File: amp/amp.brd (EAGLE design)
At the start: 99.1 x 80 mm, 81 parts, among them IC1 OPA2134PA, Q1 BC547, Q10 BC547, Q11 IRF540, Q12 IRF540, Q13 BC547, Q14 BC556, Q15 BC547, Q16 BC556, Q17 2N7000, Q18 BC547, Q19 BC547, Q2 BC556, Q20 BC547, Q21 BC547, Q22 BC547, Q23 IRF540, Q24 IRF540, Q3 BC547, Q4 BC556, Q5 2N7000, Q6 BC547, Q7 BC547, Q8 BC547, Q9 BC547

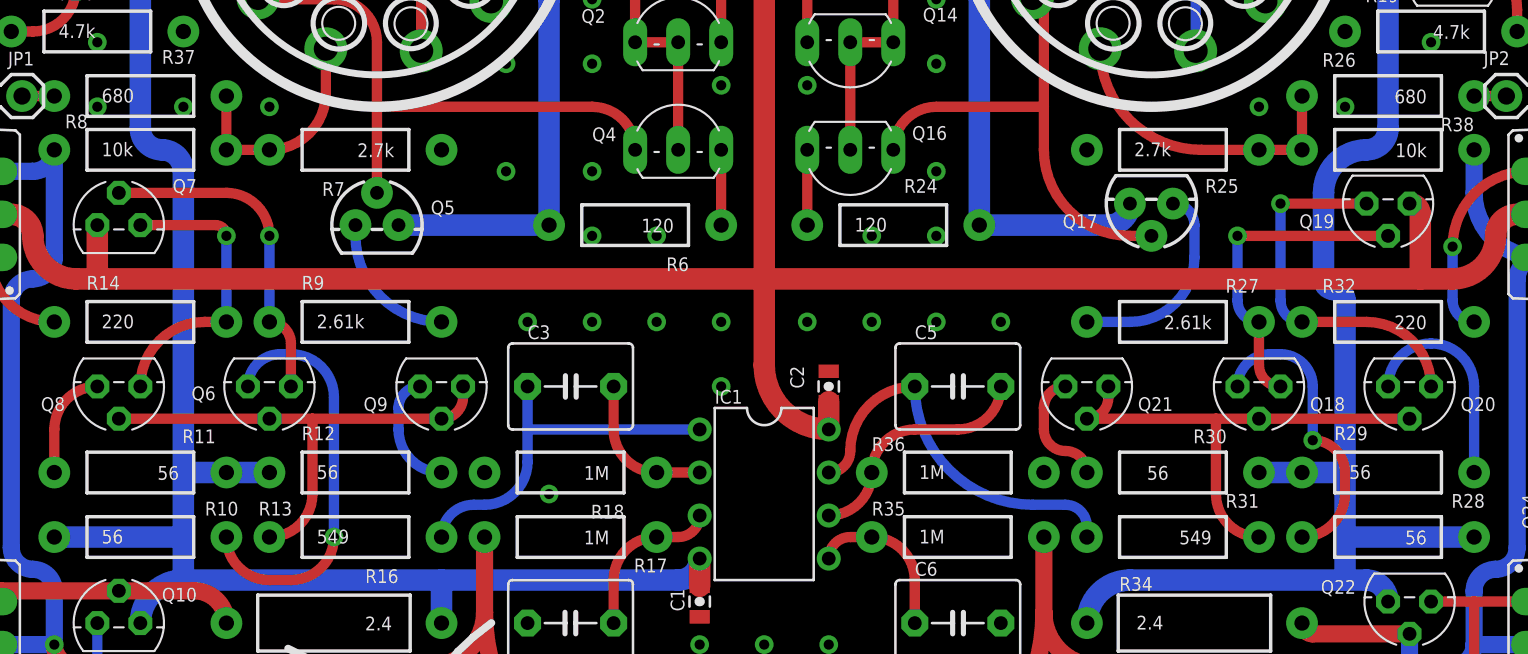
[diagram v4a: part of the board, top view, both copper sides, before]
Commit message: Some components changed
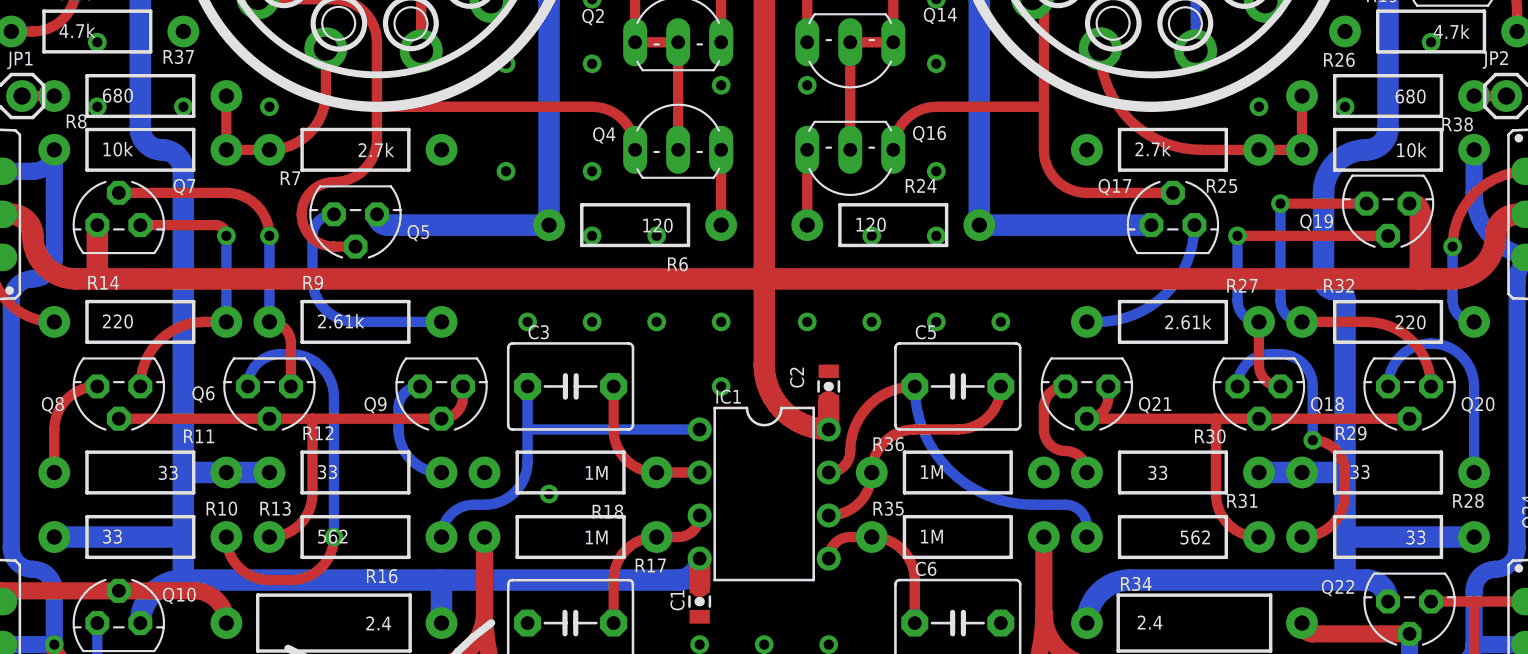
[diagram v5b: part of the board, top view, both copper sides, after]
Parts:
- Q1, Q10, Q13, Q15, Q18, Q19, Q20, Q21, Q22, Q3, Q6, Q7, Q8, Q9: value BC547 -> BC550C
- Q11, Q12, Q23, Q24: value IRF540 -> IRF510
- Q14, Q16, Q2, Q4: value BC556 -> BC560C
- Q17, Q5: value 2N7000 -> BC550C; device SparkFun-DiscreteSemi:TO-92 -> transistor-npn:TO92
- R10, R11, R12, R28, R29, R30: value 56 -> 33
- R13, R31: value 549 -> 562
- moved Q17 1.80 mm to (73.7, 38.7), turned to 0 degrees
- moved Q5 1.42 mm to (25.4, 39.4), turned to 180 degrees
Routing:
- net N$4: track 33.3 -> 40.4 mm
- net N$14: track 7.82 -> 13.0 mm
- net N$43: track 11.6 -> 8.72 mm
- net HT: track 100.9 -> 103.2 mm
